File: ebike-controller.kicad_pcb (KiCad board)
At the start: 2 copper layers, 61 parts, among them J1 Conn_01x08, J10 Conn_01x02, J2 Conn_01x08, J3 Tag Connect, J4 USB_C_Receptacle_USB2.0_14P, J5 Conn_01x02, J6 Conn_01x02, J7 Conn_01x02, J8 Conn_01x02, J9 Conn_01x02, U1 STM32F405RGTx, U2 TCAN330, U3 LM65625SRZTR, U4 LM65625SRZTR, Y2 Crystal_GND2_Small

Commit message: Snapshot before schematic review fixes
Co-Authored-By: Claude Opus 5.5 <noreply@anthropic.com>
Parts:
- added L1: 6.8uH, jackson:Inductor_SMD_7.4mmx6.6mm, F.Cu at (111.9, 98.3)
- added L2: 8.2uH, jackson:Inductor_SMD_7.4mmx6.6mm, F.Cu at (111.9, 106.0)
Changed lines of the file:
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@@
 		)
 	)
+	(footprint "jackson:Inductor_SMD_7.4mmx6.6mm"
+		(layer "F.Cu")
+		(at 111.9 98.325)
+		(property "Reference" "L1"
+			(at 0 -0.5 0)
+			(unlocked yes)
+			(layer "F.SilkS")
+			(effects
+				(font
+					(size 1 1)
+					(thickness 0.1)
+				)
+			)
+		)
+		(property "Value" "6.8uH"
+			(at 0 1 0)
+			(unlocked yes)
+			(layer "F.Fab")
+			(effects
+				(font
+					(size 1 1)
+					(thickness 0.15)
+				)
+			)
+		)
+		(property "Datasheet" ""
+			(at 0 0 0)
+			(unlocked yes)
+			(layer "F.Fab")
+			(hide yes)
+			(effects
+				(font
+					(size 1 1)
+					(thickness 0.15)
+				)
+			)
+		)
+		(property "Description" "Inductor"
+			(at 0 0 0)
+			(unlocked yes)
+			(layer "F.Fab")
+			(hide yes)
+			(effects
+				(font
+					(size 1 1)
+					(thickness 0.15)
+				)
+			)
+		)
+		(property "LCSC Part Number" "C51933839"
+			(at 0 0 0)
+			(unlocked yes)
+			(layer "F.Fab")
+			(hide yes)
+			(effects
+				(font
+					(size 1 1)
+					(thickness 0.15)
+				)
+			)
+		)
+		(property ki_fp_filters "Choke_* *Coil* Inductor_* L_*")
+		(sheetname "/Power/")
+		(sheetfile "power.kicad_sch")
+		(units
+			(unit
+				(name "A")
+				(pins "1" "2")
+			)
+		)
+		(attr smd)
+		(duplicate_pad_numbers_are_jumpers no)
+		(fp_rect
+			(start -3.7 -3.3)
+			(end 3.7 3.3)
+			(stroke
+				(width 0.05)
+				(type solid)
+			)
+			(fill no)
+			(layer "F.CrtYd")
+		)
+		(fp_text user "${REFERENCE}"
+			(at 0 2.5 0)
+			(unlocked yes)
+			(layer "F.Fab")
+			(effects
+				(font
+					(size 1 1)
+					(thickness 0.15)
+				)
+			)
+		)
+		(pad "1" smd roundrect
+			(at -3.025 0 90)
+			(size 3.5 2.35)
+			(layers "F.Cu" "F.Mask" "F.Paste")
+			(roundrect_rratio 0.15)
+			(net "Net-(U3-SW1)")
+			(pinfunction "1_1")
+			(pintype "passive")
+		)
+		(pad "2" smd roundrect
+			(at 3.025 0 90)
+			(size 3.5 2.35)
+			(layers "F.Cu" "F.Mask" "F.Paste")
+			(roundrect_rratio 0.15)
+			(net "+3V3")
+			(pinfunction "2_2")
+			(pintype "passive")
+		)
+		(embedded_fonts no)
+	)
 	(footprint "Connector_Molex:Molex_Micro-Fit_3.0_43650-0200_1x02_P3.00mm_Horizontal"
 		(layer "F.Cu")
@@
 				(name "A")
 				(pins "7" "60" "5" "6" "54" "8" "9" "10" "11" "24" "25" "37" "38" "39"
-					"40" "51" "52" "53" "2" "3" "4" "31" "47" "1" "19" "32" "63" "18" "48"
+					"40" "51" "52" "53" "2" "3" "4" "31" "47" "1" "19" "32" "18" "63" "48"
 					"12" "64" "13" "14" "15" "16" "17" "20" "21" "22" "23" "41" "42" "43"
 					"44" "45" "46" "49" "50" "26" "27" "28" "55" "56" "57" "58" "59" "61"
@@
 		)
 	)
+	(footprint "jackson:Inductor_SMD_7.4mmx6.6mm"
+		(layer "F.Cu")
+		(at 111.9 105.975)
+		(property "Reference" "L2"
+			(at 0 -0.5 0)
+			(unlocked yes)
+			(layer "F.SilkS")
+			(effects
+				(font
+					(size 1 1)
+					(thickness 0.1)
+				)
+			)
+		)
+		(property "Value" "8.2uH"
+			(at 0 1 0)
+			(unlocked yes)
+			(layer "F.Fab")
+			(effects
+				(font
+					(size 1 1)
+					(thickness 0.15)
+				)
+			)
+		)
+		(property "Datasheet" ""
+			(at 0 0 0)
+			(unlocked yes)
+			(layer "F.Fab")
+			(hide yes)
+			(effects
+				(font
+					(size 1 1)
+					(thickness 0.15)
+				)
+			)
+		)
+		(property "Description" "Inductor"
+			(at 0 0 0)
+			(unlocked yes)
+			(layer "F.Fab")
+			(hide yes)
+			(effects
+				(font
+					(size 1 1)
+					(thickness 0.15)
+				)
+			)
+		)
+		(property "LCSC Part Number" "C53462990"
+			(at 0 0 0)
+			(unlocked yes)
+			(layer "F.Fab")
+			(hide yes)
+			(effects
+				(font
+					(size 1 1)
+					(thickness 0.15)
+				)
+			)
+		)
+		(property ki_fp_filters "Choke_* *Coil* Inductor_* L_*")
+		(sheetname "/Power/")
+		(sheetfile "power.kicad_sch")
+		(units
+			(unit
+				(name "A")
+				(pins "1" "2")
+			)
+		)
+		(attr smd)
+		(duplicate_pad_numbers_are_jumpers no)
+		(fp_rect
+			(start -3.7 -3.3)
+			(end 3.7 3.3)
+			(stroke
+				(width 0.05)
+				(type solid)
+			)
+			(fill no)
+			(layer "F.CrtYd")
+		)
+		(fp_text user "${REFERENCE}"
+			(at 0 2.5 0)
+			(unlocked yes)
+			(layer "F.Fab")
+			(effects
+				(font
+					(size 1 1)
+					(thickness 0.15)
+				)
+			)
+		)
+		(pad "1" smd roundrect
+			(at -3.025 0 90)
+			(size 3.5 2.35)
+			(layers "F.Cu" "F.Mask" "F.Paste")
+			(roundrect_rratio 0.15)
+			(net "Net-(U4-SW1)")
+			(pinfunction "1_1")
+			(pintype "passive")
+		)
+		(pad "2" smd roundrect
+			(at 3.025 0 90)
+			(size 3.5 2.35)
+			(layers "F.Cu" "F.Mask" "F.Paste")
+			(roundrect_rratio 0.15)
+			(net "+5V")
+			(pinfunction "2_2")
+			(pintype "passive")
+		)
+		(embedded_fonts no)
+	)
 	(footprint "Resistor_SMD:R_0402_1005Metric"

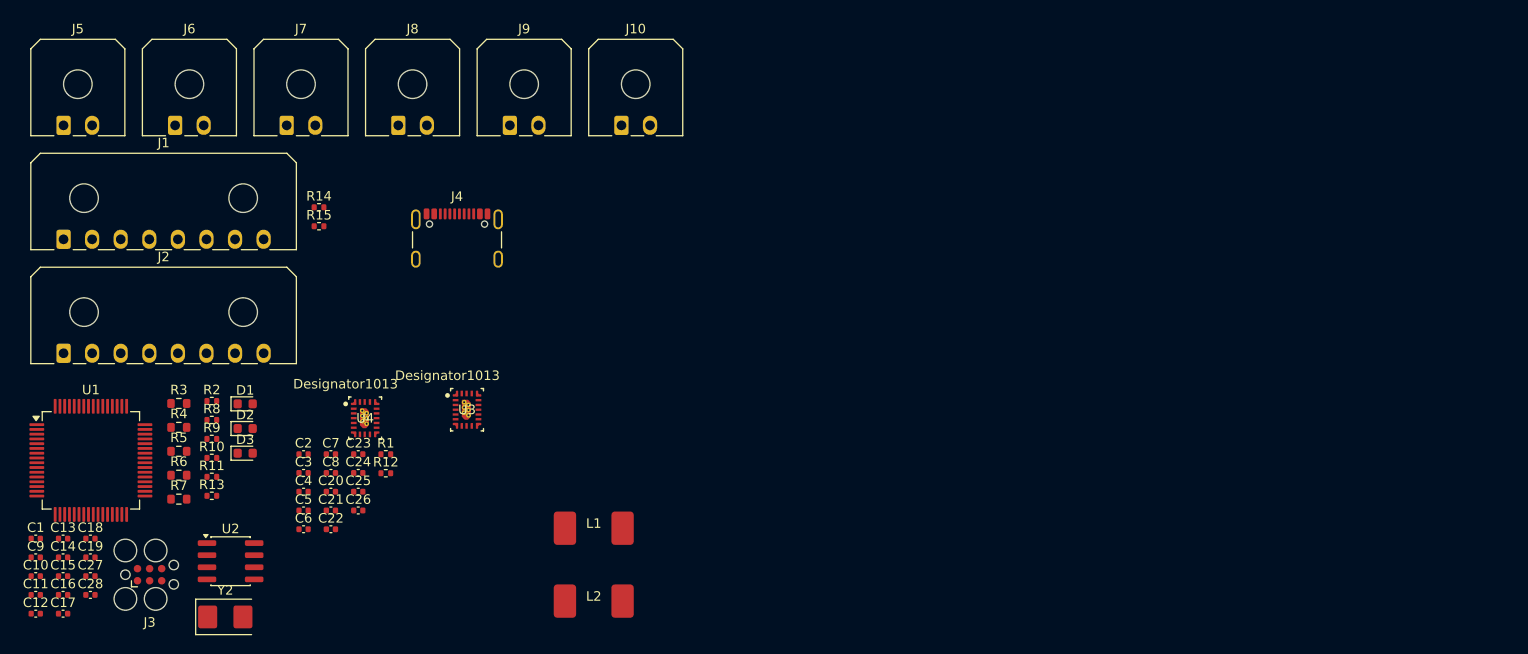
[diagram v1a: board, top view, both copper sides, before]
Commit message: Update PCB and schematics after review fixes
Co-Authored-By: Claude Opus 5.5 <noreply@anthropic.com>
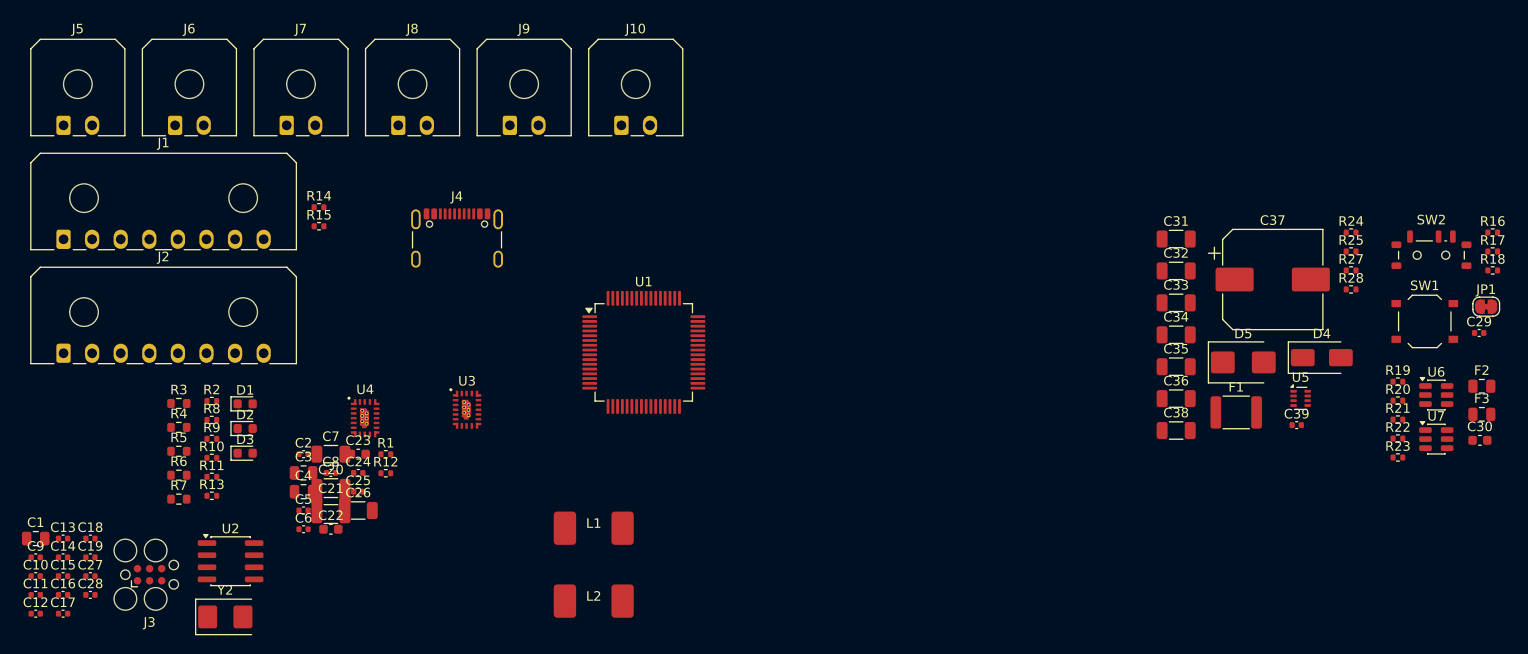
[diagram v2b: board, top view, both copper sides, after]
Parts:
- added C29: 100nF, Capacitor_SMD:C_0402_1005Metric, F.Cu at (204.8, 77.8)
- added C30: 4.7uF, Capacitor_SMD:C_0603_1608Metric, F.Cu at (204.9, 89.1)
- added C31: 47uF, Capacitor_SMD:C_1206_3216Metric, F.Cu at (173.0, 68.0)
- added C32: 47uF, Capacitor_SMD:C_1206_3216Metric, F.Cu at (173.0, 71.3)
- added C33: 47uF, Capacitor_SMD:C_1206_3216Metric, F.Cu at (173.0, 74.7)
- added C34: 47uF, Capacitor_SMD:C_1206_3216Metric, F.Cu at (173.0, 78.0)
- added C35: 47uF, Capacitor_SMD:C_1206_3216Metric, F.Cu at (173.0, 81.4)
- added C36: 47uF, Capacitor_SMD:C_1206_3216Metric, F.Cu at (173.0, 84.7)
- added C37: 47uF 100V, Capacitor_SMD:CP_Elec_10x10, F.Cu at (183.2, 72.2)
- added C38: 47uF, Capacitor_SMD:C_1206_3216Metric, F.Cu at (173.0, 88.1)
- added C39: 1uF, Capacitor_SMD:C_0402_1005Metric, F.Cu at (185.7, 87.5)
- added D4: SS210, Diode_SMD:D_SMA, F.Cu at (188.3, 80.4)
- added D5: SMBJ43A, Diode_SMD:D_SMB, F.Cu at (180.1, 80.9)
- added F1: 500mA 60V, Fuse:Fuse_1812_4532Metric, F.Cu at (179.3, 86.2)
- added F2: 500mA, Fuse:Fuse_0805_2012Metric, F.Cu at (205.1, 83.4)
- added F3: 350mA, Fuse:Fuse_0805_2012Metric, F.Cu at (205.1, 86.4)
- added JP1: TERM, Jumper:SolderJumper-2_P1.3mm_Bridged_RoundedPad1.0x1.5mm, F.Cu at (205.6, 75.1)
- added R16: 10k, Resistor_SMD:R_0402_1005Metric, F.Cu at (206.2, 67.3)
- added R17: 22k, Resistor_SMD:R_0402_1005Metric, F.Cu at (206.2, 69.3)
- added R18: 33k, Resistor_SMD:R_0402_1005Metric, F.Cu at (206.2, 71.3)
- added R19: 100R, Resistor_SMD:R_0402_1005Metric, F.Cu at (196.3, 82.9)
- added R20: 100R, Resistor_SMD:R_0402_1005Metric, F.Cu at (196.3, 84.9)
- added R21: 100R, Resistor_SMD:R_0402_1005Metric, F.Cu at (196.3, 86.9)
- added R22: 100R, Resistor_SMD:R_0402_1005Metric, F.Cu at (196.3, 88.9)
- added R23: 100R, Resistor_SMD:R_0402_1005Metric, F.Cu at (196.3, 90.9)
- added R24: 232k, Resistor_SMD:R_0402_1005Metric, F.Cu at (191.4, 67.3)
- added R25: 10k, Resistor_SMD:R_0402_1005Metric, F.Cu at (191.4, 69.3)
- added R27: 33k, Resistor_SMD:R_0402_1005Metric, F.Cu at (191.4, 71.3)
- added R28: 10k, Resistor_SMD:R_0402_1005Metric, F.Cu at (191.4, 73.3)
- added SW1: RESET, Button_Switch_SMD:SW_Push_1P1T_XKB_TS-1187A, F.Cu at (199.1, 76.6)
- added SW2: BOOT0, Button_Switch_SMD:SW_SPDT_Shouhan_MSK12C02, F.Cu at (199.8, 69.7)
- added U5: TPS2116DRLR, Package_TO_SOT_SMD:SOT-583-8, F.Cu at (186.1, 84.7)
- added U6: USBLC6-2SC6, Package_TO_SOT_SMD:SOT-23-6, F.Cu at (200.3, 84.3)
- added U7: SP0505BAHT, Package_TO_SOT_SMD:SOT-23-6, F.Cu at (200.3, 89.0)
- C1, C3, C4: footprint Capacitor_SMD:C_0402_1005Metric -> Capacitor_SMD:C_0805_2012Metric
- C11, C12, C13, C14, C15, C16: value 100nf -> 100nF
- C18, C19: value 15pF -> 33pF
- C2, C24: value 0.1uF -> 100nF
- C20, C21: footprint Capacitor_SMD:C_0402_1005Metric -> Capacitor_SMD:C_1210_3225Metric
- C22, C23: footprint Capacitor_SMD:C_0402_1005Metric -> Capacitor_SMD:C_0603_1608Metric
- C26: value 55uF -> 47uF; footprint Capacitor_SMD:C_0402_1005Metric -> Capacitor_SMD:C_1206_3216Metric
- C7: value 94uF -> 47uF; footprint Capacitor_SMD:C_0402_1005Metric -> Capacitor_SMD:C_1206_3216Metric
- D2: value GREEN -> Y-GRN
- J1, J2: value Conn_01x08 -> Micro-Fit 1x08
- J10, J5, J6, J7, J8, J9: value Conn_01x02 -> Micro-Fit 1x02
- J4: value USB_C_Receptacle_USB2.0_14P -> USB4105-GF-A
- L2: value 8.2uH -> 10uH
- R10: value 1k -> 68R
- R2: value 100k -> 1k
- U1: value STM32F405RGTx -> STM32F405RGT6
- U2: value TCAN330 -> TCAN330DR
- U3, U4: value LM65625SRZTR -> LM65625SRZTRQ1; footprint Jackson:RZT0020A-MFG -> ebike-controller:TI_RZT0020A
- Y2: value Crystal_GND2_Small -> 8MHz 20pF
- moved U1 59.1 mm to (117.2, 79.9)
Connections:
- net /MCU/OSC32_IN renamed /MCU/HSE_IN
- net /MCU/OSC32_OUT renamed /MCU/HSE_OUT
- C11 pad 1: /MCU/NRST -> NRST
- C20 pad 1: VCC -> GND
- C20 pad 2: Net-(U4-EN/UVLO) -> /Power/VIN_PROT
- C21 pad 1: VCC -> GND
- C21 pad 2: Net-(U4-EN/UVLO) -> /Power/VIN_PROT
- C22 pad 1: VCC -> GND
- C22 pad 2: Net-(U4-EN/UVLO) -> /Power/VIN_PROT
- C23 pad 1: VCC -> GND
- C23 pad 2: Net-(U4-EN/UVLO) -> /Power/VIN_PROT
- C26 pad 1: +5V -> /Power/5V_BUCK
- C27 pad 1: GNDA -> GND
- C28 pad 1: GNDA -> GND
- C3 pad 1: VCC -> GND
- C3 pad 2: Net-(U3-EN/UVLO) -> +5V
- C4 pad 1: VCC -> GND
- C4 pad 2: Net-(U3-EN/UVLO) -> +5V
- C5 pad 1: VCC -> GND
- C5 pad 2: Net-(U3-EN/UVLO) -> +5V
- C6 pad 1: VCC -> GND
- C6 pad 2: Net-(U3-EN/UVLO) -> +5V
- J10 pad 1: +5V -> /IO/+5V_EXT
- J2 pad 1: +5V -> /IO/+5V_EXT
- J2 pad 2: +3V3 -> /IO/+3V3_EXT
- J2 pad 3: /IO/GPIO0 -> /IO/EXT0
- J2 pad 4: /IO/GPIO1 -> /IO/EXT1
- J2 pad 5: /IO/GPIO2 -> /IO/EXT2
- J2 pad 6: /IO/GPIO3 -> /IO/EXT3
- J2 pad 7: /IO/GPIO4 -> /IO/EXT4
- J3 pad 3: /MCU/NRST -> NRST
- J4 pad A4: +5V -> VBUS
- J4 pad A9: +5V -> VBUS
- J4 pad B4: +5V -> VBUS
- J4 pad B9: +5V -> VBUS
- L2 pad 2: +5V -> /Power/5V_BUCK
- R1 pad 1: /Power/LM656_3V3_VCC -> +3V3
- R1 pad 2: Net-(U3-PG) -> NRST
- R8 pad 2: /IO/CAN_L -> Net-(JP1-B)
- U1 pad 12: GNDA -> GND
- U1 pad 42: unconnected-(U1-PA9-Pad42) -> /MCU/VBUS_SENSE
- U1 pad 44: /MCU/USB.DM -> /IO/USB.DM
- U1 pad 45: /MCU/USB.DP -> /IO/USB.DP
- U1 pad 7: /MCU/NRST -> NRST
- U2 pad 5: unconnected-(U2-SHDN-Pad5) -> GND
- U2 pad 8: unconnected-(U2-S-Pad8) -> GND
- U3 pad 11: Net-(U3-EN/UVLO) -> +5V
- U3 pad 17: Net-(U3-EN/UVLO) -> +5V
- U3 pad 2: Net-(U3-PG) -> NRST
- U3 pad 21: (no net) -> GND
- U3 pad 7: Net-(U3-EN/UVLO) -> +5V
- U4 pad 11: Net-(U4-EN/UVLO) -> /Power/VIN_PROT
- U4 pad 17: Net-(U4-EN/UVLO) -> /Power/VIN_PROT
- U4 pad 20: +5V -> /Power/5V_BUCK
- U4 pad 21: (no net) -> GND
- U4 pad 7: Net-(U4-EN/UVLO) -> /Power/U4_EN
- Y2 pad 2: GND -> Net-(C19-Pad1)
